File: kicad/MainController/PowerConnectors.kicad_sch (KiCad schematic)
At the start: 27 parts, among them J11 Pwr, J4 H-Bridge, J5 Lamp, J7 RGB, J8 Winch, J9 Motor, Q1 BC547, Q10 BUZ11, Q2 BUZ11, Q3 BC547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

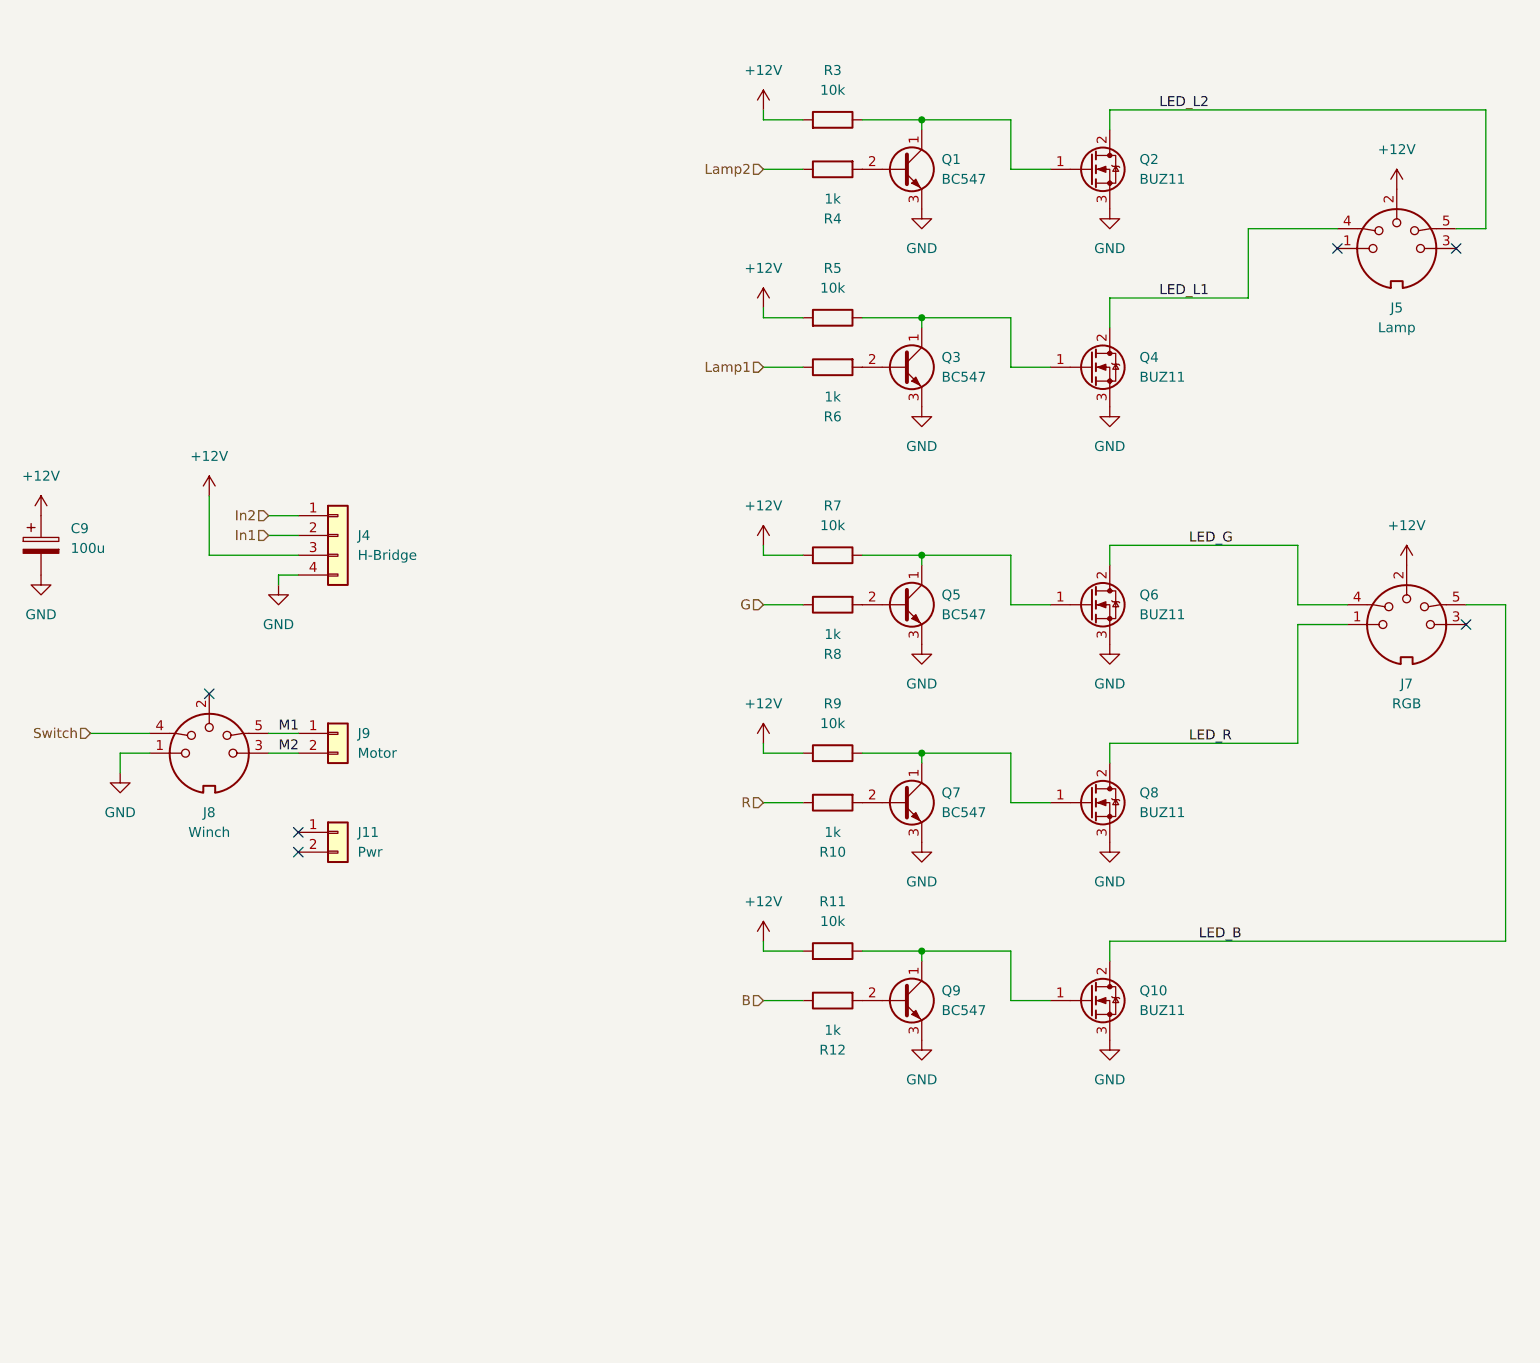
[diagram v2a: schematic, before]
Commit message: Updated main controller for digital RGB strip
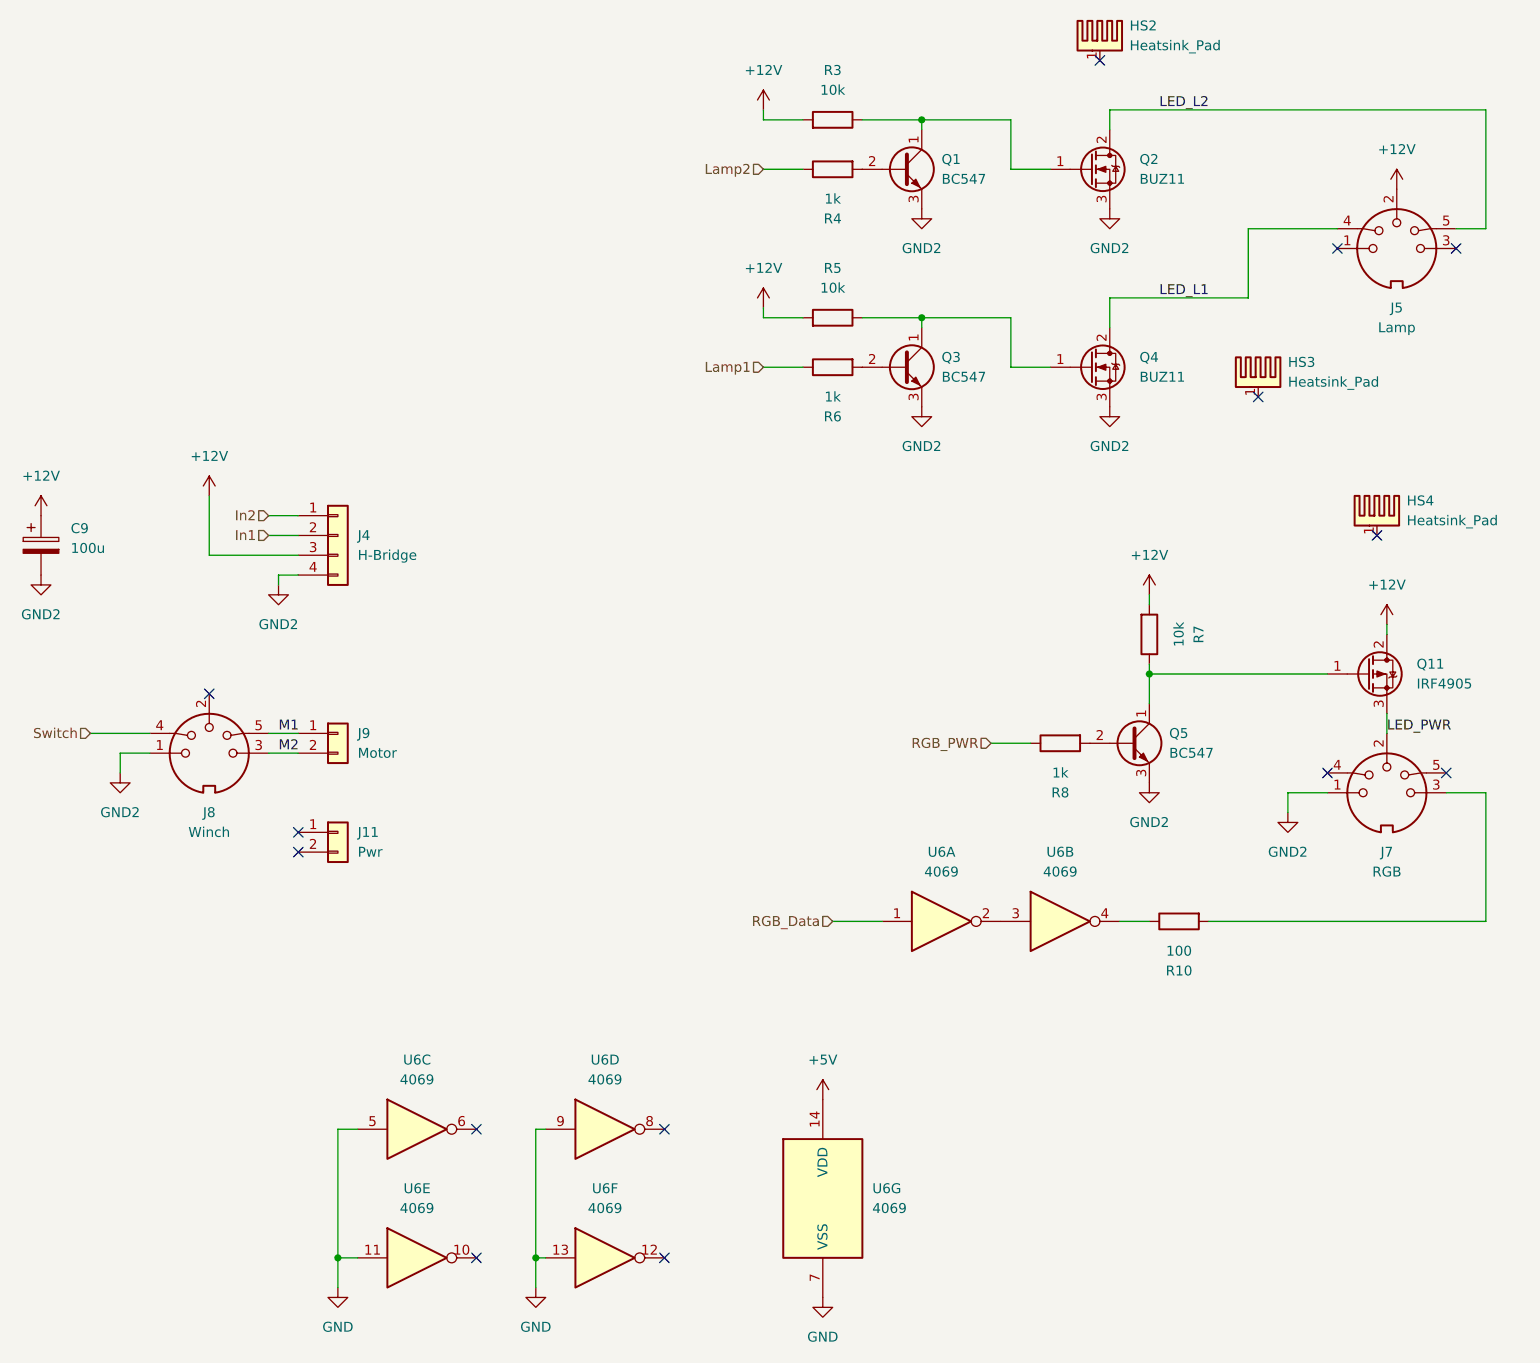
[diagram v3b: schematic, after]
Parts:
- removed Q10, Q6, Q8: BUZ11, Package_TO_SOT_THT:TO-220-3_Vertical, symbol Transistor_FET:BUZ11
- removed Q7, Q9: BC547, Custom_Footprints:TO-92_Milling, symbol Transistor_BJT:BC547
- removed R11, R9: 10k, Resistor_THT:R_Axial_DIN0207_L6.3mm_D2.5mm_P2.54mm_Vertical, symbol Device:R
- removed R12: 1k, Resistor_THT:R_Axial_DIN0207_L6.3mm_D2.5mm_P10.16mm_Horizontal, symbol Device:R
- added HS2, HS3, HS4: Heatsink_Pad, Custom_Heatsinks:Heatsink_Aavid_TO-220_H12.7mm, symbol Mechanical:Heatsink_Pad
- added Q11: IRF4905, Package_TO_SOT_THT:TO-220-3_Vertical, symbol Transistor_FET:IRF4905
- added U6: 4069, Package_DIP:DIP-14_W7.62mm, symbol 4xxx:4069
- R10: value 1k -> 100
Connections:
- net +12V: now also Q11.2 (D); no longer J7.2
- net GND: now also U6.11, U6.13, U6.5, U6.7 (VSS), U6.9; no longer C9.2, J4.4 (Pin_4), J8.1, Q1.3 (E), Q2.3 (S), Q3.3 (E), Q4.3 (S), Q5.3 (E)
- net at J7.3: now also R10.2
- net at Q5.1 (C), R7.1: now also Q11.1 (G)
- net G renamed RGB_PWR
- net LED_B: no longer names the net of J7.5
- net LED_G: no longer names the net of J7.4
- net LED_R renamed GND2
- net GND2: now also C9.2, J4.4 (Pin_4), J8.1, Q1.3 (E), Q2.3 (S), Q3.3 (E), Q4.3 (S), Q5.3 (E)
- net R: no longer names the net of R10.1
- net R: now also U6.4
- new net: U6.2, U6.3
- new net +5V: U6.14 (VDD)
- new net LED_PWR: J7.2, Q11.3 (S)
- new net RGB_Data: U6.1
- no-connect marks 6 -> 14
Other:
- moved on the sheet: J7, Q5, R7, R8

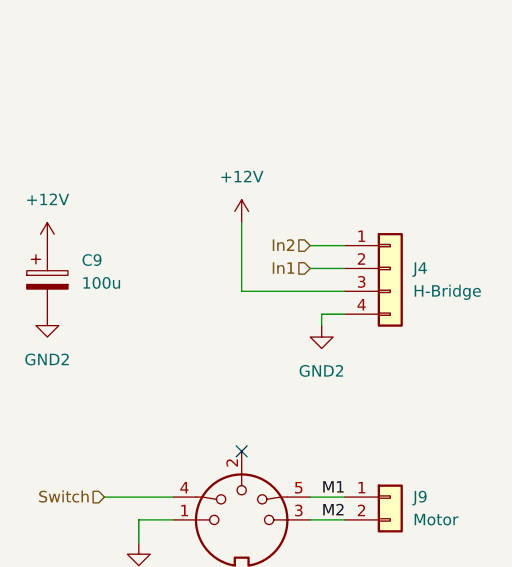
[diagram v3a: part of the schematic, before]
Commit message: Fixed footprints for MainController board
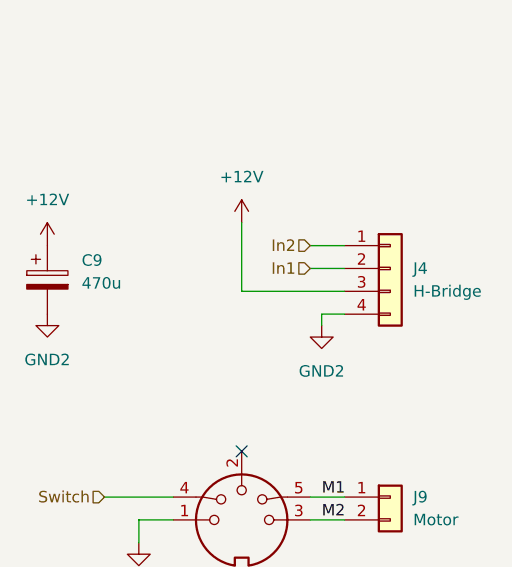
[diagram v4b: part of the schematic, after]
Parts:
- C9: value 100u -> 470u; footprint Capacitor_THT:CP_Radial_D7.5mm_P2.50mm -> Capacitor_THT:CP_Radial_D10.0mm_P5.00mm
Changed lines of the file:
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@@
 			)
 		)
-		(property "Value" "100u"
+		(property "Value" "470u"
 			(at 54.61 88.0109 0)
 			(effects
@@
 			)
 		)
-		(property "Footprint" "Capacitor_THT:CP_Radial_D7.5mm_P2.50mm"
+		(property "Footprint" "Capacitor_THT:CP_Radial_D10.0mm_P5.00mm"
 			(at 51.7652 91.44 0)
 			(effects

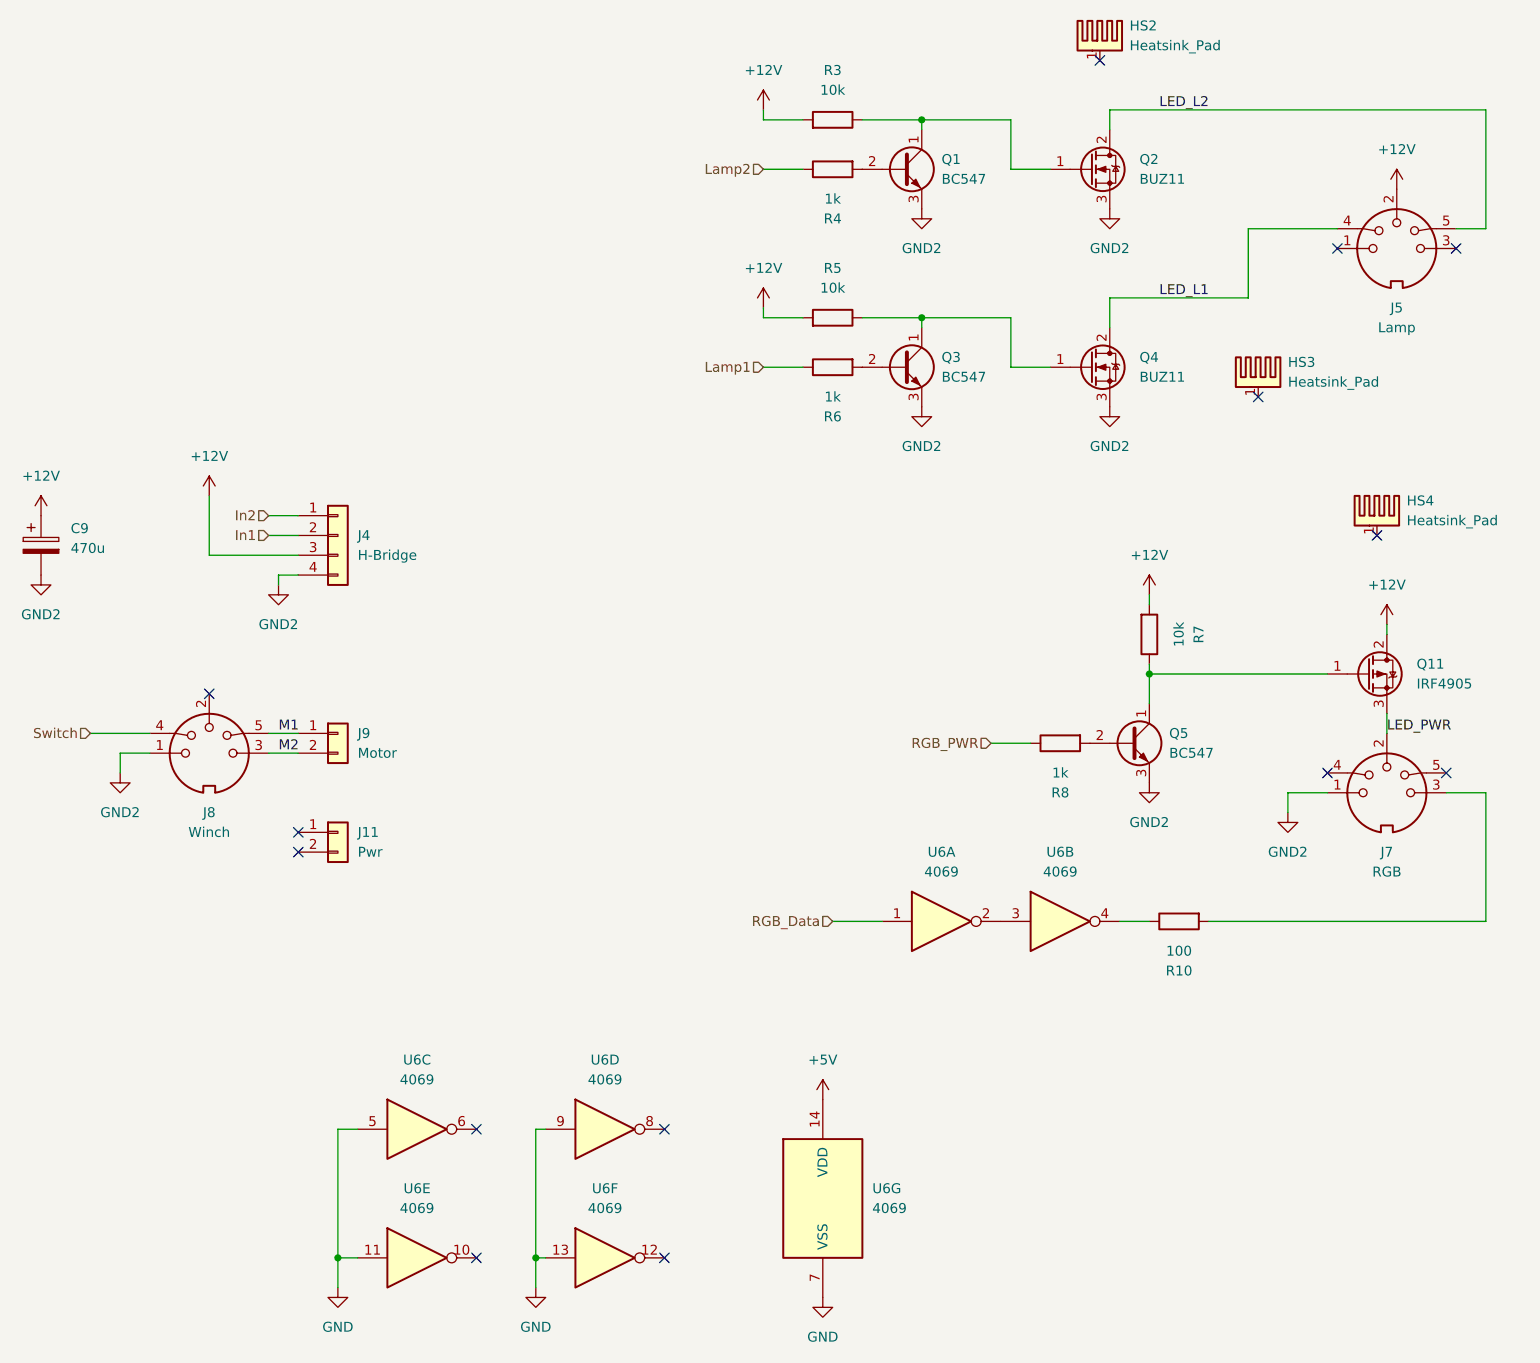
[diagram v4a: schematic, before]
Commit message: Fixed MainController LED power and data drivers
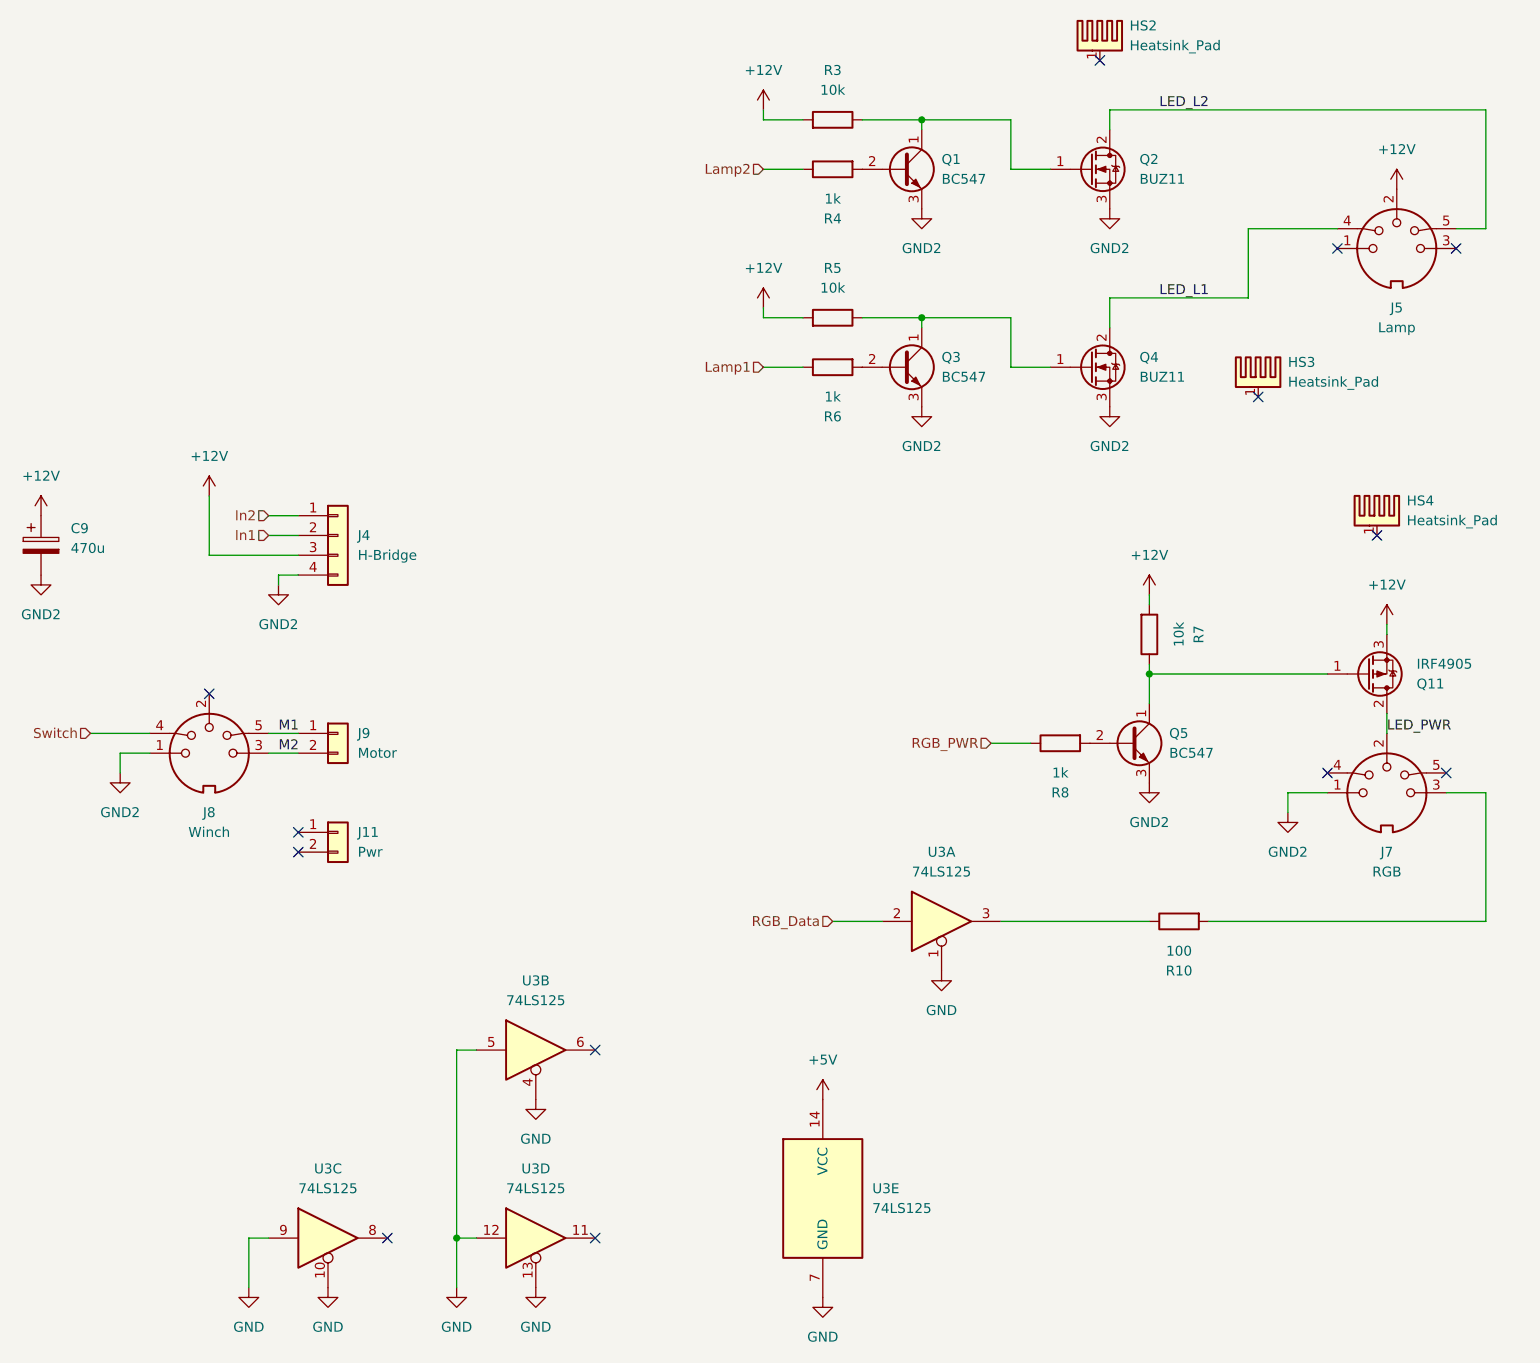
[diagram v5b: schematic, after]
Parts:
- removed U6: 4069, Package_DIP:DIP-14_W7.62mm, symbol 4xxx:4069
- added U3: 74LS125, Package_DIP:DIP-14_W7.62mm, symbol 74xx:74LS125
- R7: footprint Resistor_THT:R_Axial_DIN0207_L6.3mm_D2.5mm_P2.54mm_Vertical -> Resistor_THT:R_Axial_DIN0207_L6.3mm_D2.5mm_P10.16mm_Horizontal
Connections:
- net +12V: now also Q11.3 (S); no longer Q11.2 (D)
- net +5V: now also U3.14 (VCC)
- net GND: now also U3.1, U3.10, U3.12, U3.13, U3.4, U3.5, U3.7 (GND), U3.9
- net LED_PWR: now also Q11.2 (D); no longer Q11.3 (S)
- net RGB_Data: now also U3.2
- net at R10.1: now also U3.3
- no-connect marks 14 -> 13
